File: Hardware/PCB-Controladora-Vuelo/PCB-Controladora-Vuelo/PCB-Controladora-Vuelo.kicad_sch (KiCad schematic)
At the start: 14 parts, among them J1 Jumper Serial, J2 CONN, U1 MPU-5060, U2 ESP32-DEVKIT-V1, U2 Nrf24l01, U3 AMS1117-3.3

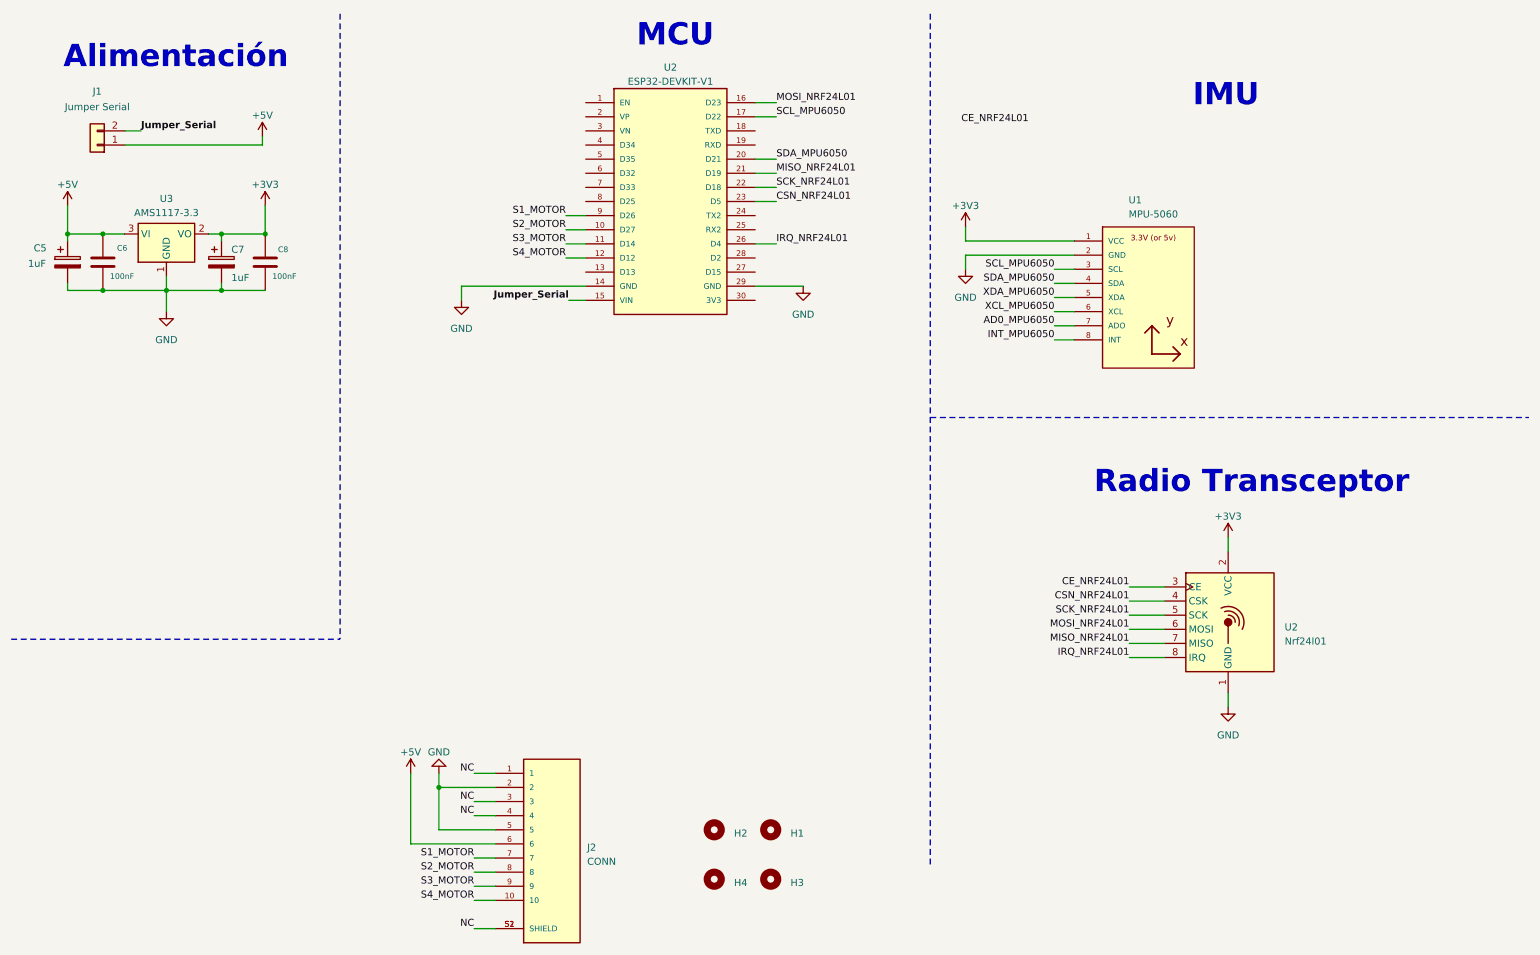
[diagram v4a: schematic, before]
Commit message: subo cambios hechos en legui solucione mpu y lugar esp32 mal Footprints
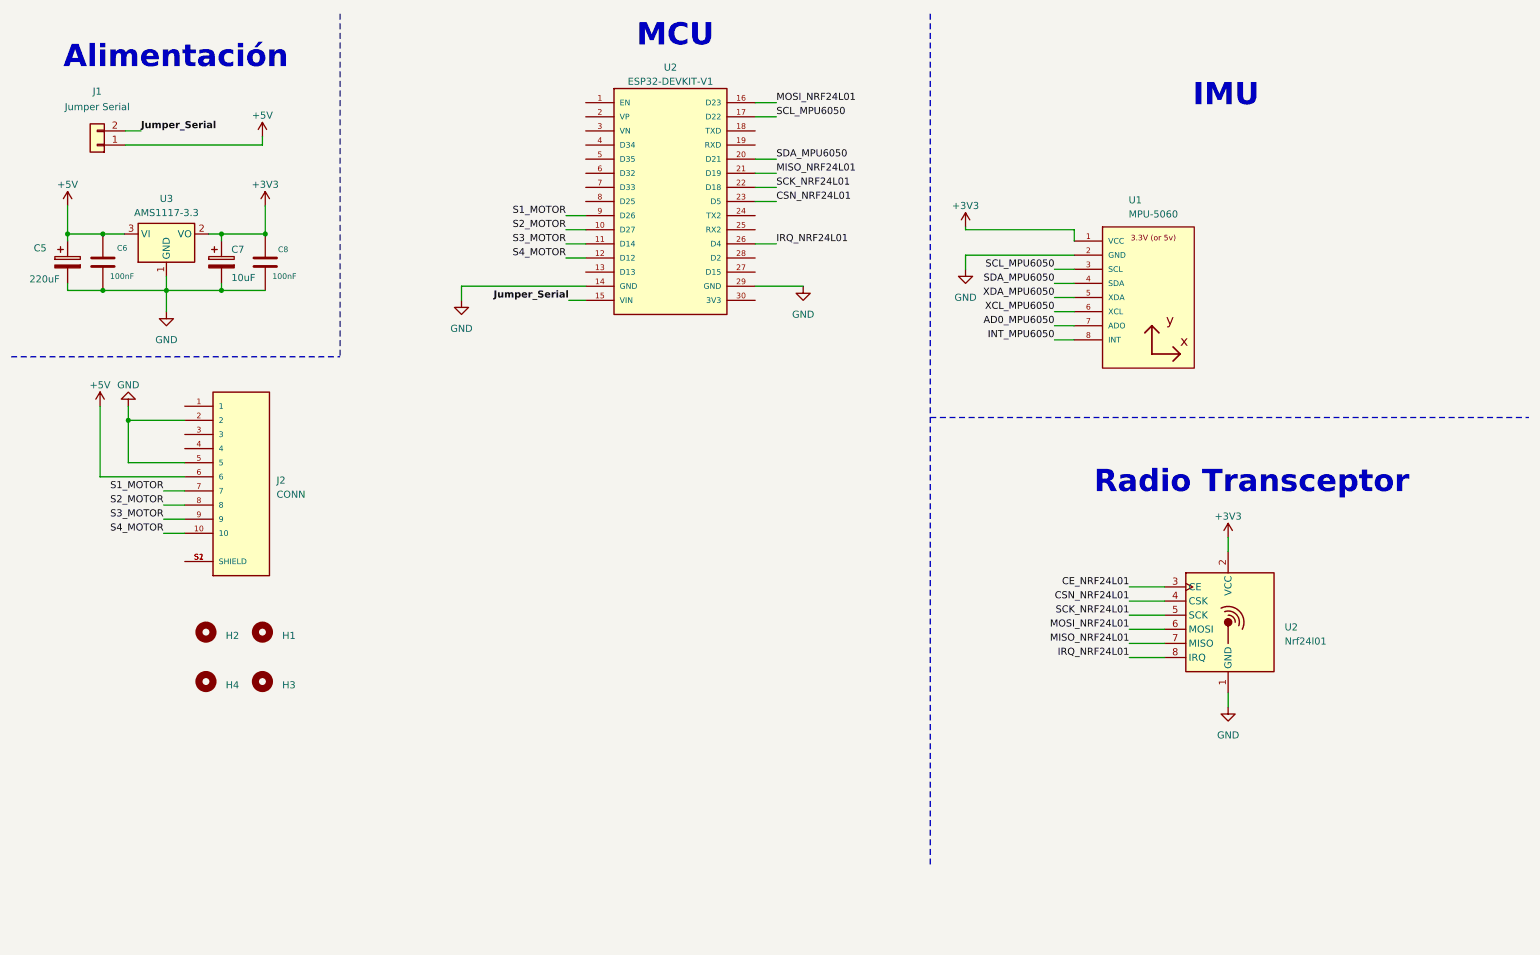
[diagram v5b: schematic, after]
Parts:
- C5: value 1uF -> 220uF
- C7: value 1uF -> 10uF
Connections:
- removed net NC: J2.1, J2.3, J2.4, J2.S1 (SHIELD), J2.S2 (SHIELD)
- new net: J2.S1 (SHIELD), J2.S2 (SHIELD)
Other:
- moved on the sheet: H1, H2, H3, H4, J2

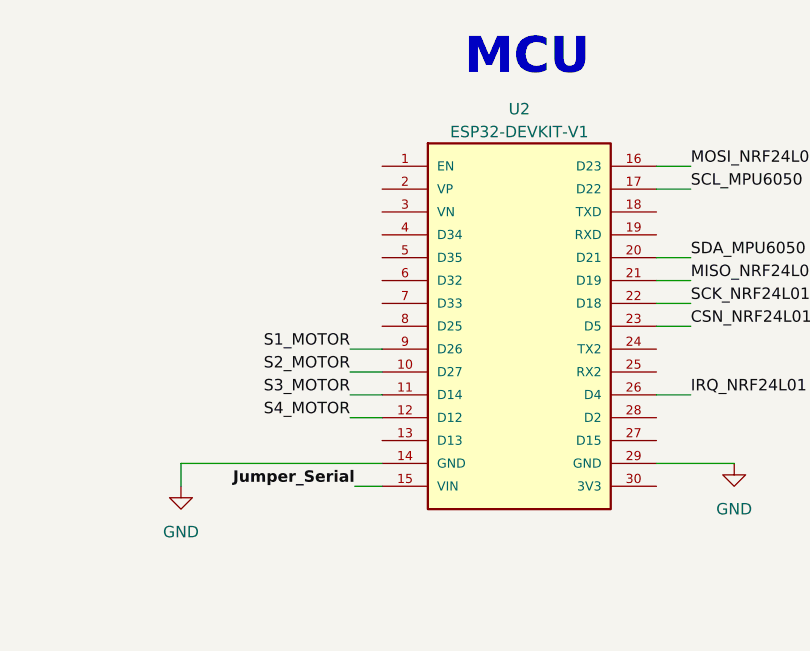
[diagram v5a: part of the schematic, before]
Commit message: Realice cambios de huella ESP32 y Symbol
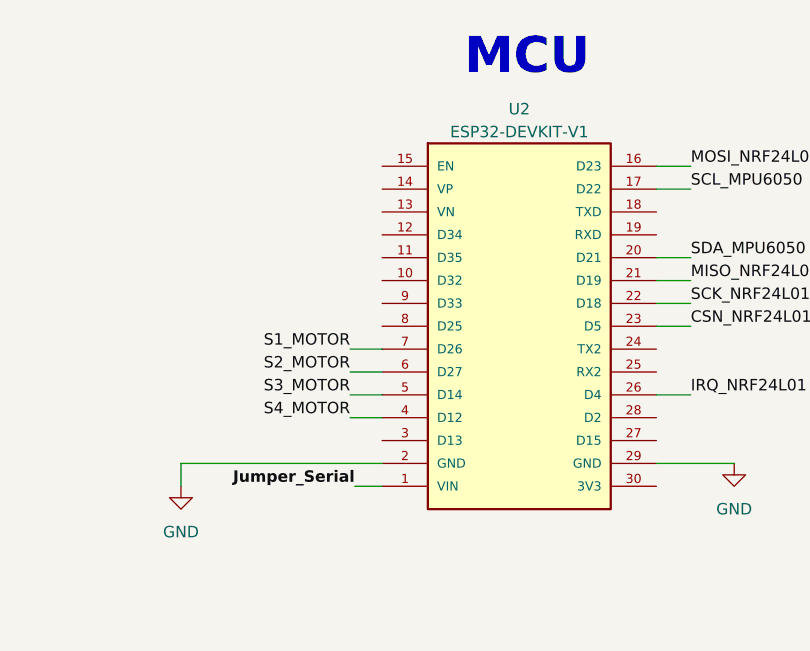
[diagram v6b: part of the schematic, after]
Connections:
- net GND: now also U2.2 (GND); no longer U2.14 (GND)
- net Jumper_Serial: now also U2.1 (VIN); no longer U2.15 (VIN)
- net S1_MOTOR: now also U2.7 (D26); no longer U2.9 (D26)
- net S2_MOTOR: now also U2.6 (D27); no longer U2.10 (D27)
- net S3_MOTOR: now also U2.5 (D14); no longer U2.11 (D14)
- net S4_MOTOR: now also U2.4 (D12); no longer U2.12 (D12)
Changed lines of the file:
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@@
       (effects (font (size 1.27 1.27)))
     )
-    (property "Footprint" "Footprints:ESP32-DEVKIT-V1-30Pines" (at 131.826 48.26 0)
+    (property "Footprint" "Footprints:ESP32-DEVKIT-V1-30Pines" (at 134.366 41.91 0)
       (effects (font (size 1.27 1.27)) (justify bottom) hide)
     )

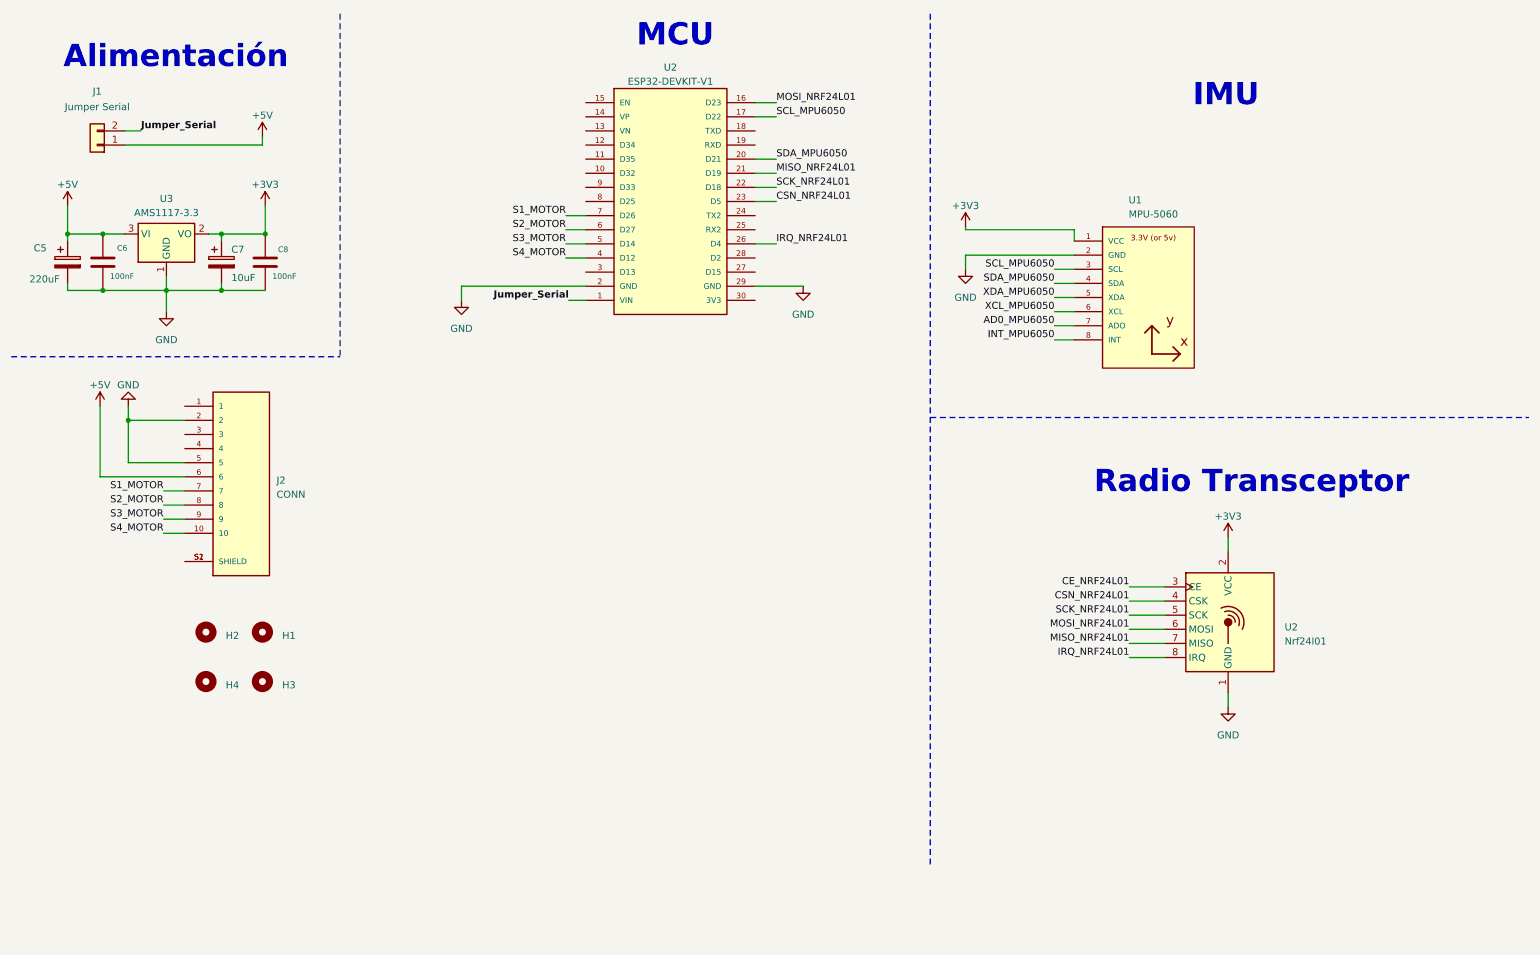
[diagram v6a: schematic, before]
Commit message: muchos cambios leer saque todos los NC y coloque X ya que al poner etiquetas nc reconoce como que debe haber una conexion entre ellos y nqv tambien digamos que hice una buena 1ra parte de pcb, que se debe corregir y mirar todo mas a detalle , faltan definir unos pines para ver si es necesario para la primera prueba xD
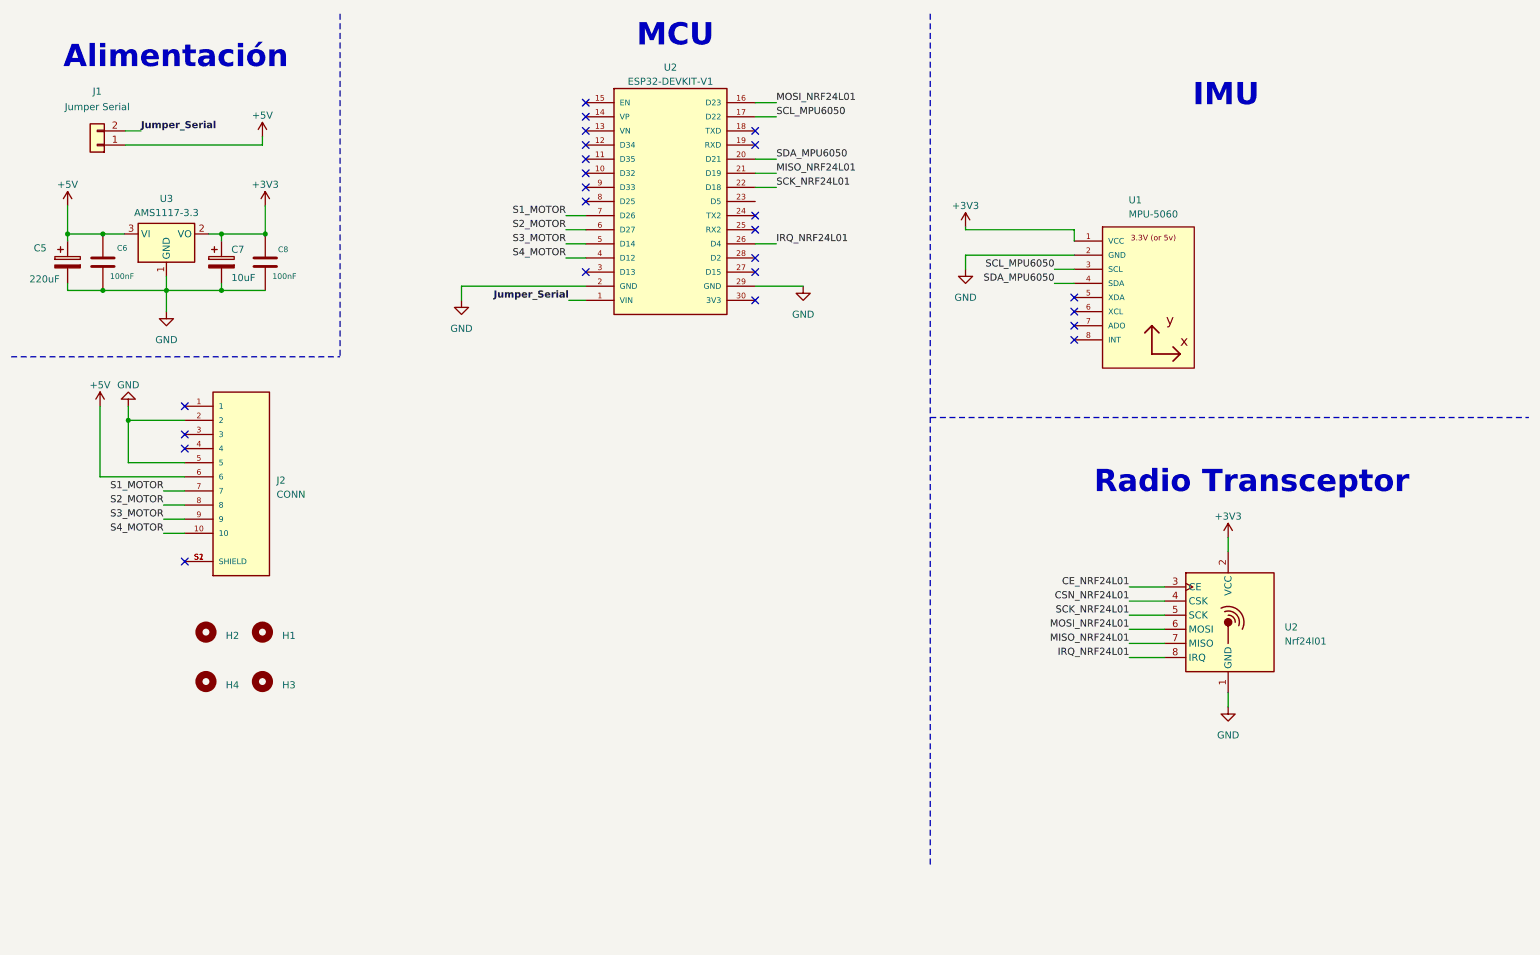
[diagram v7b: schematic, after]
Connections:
- net CSN_NRF24L01: no longer U2.23 (D5)
- net AD0_MPU6050: no longer names the net of U1.7 (ADO)
- net INT_MPU6050: no longer names the net of U1.8 (INT)
- net XCL_MPU6050: no longer names the net of U1.6 (XCL)
- net XDA_MPU6050: no longer names the net of U1.5 (XDA)
- no-connect marks 0 -> 24
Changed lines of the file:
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@@
   (junction (at 49.784 51.562) (diameter 0) (color 0 0 0 0)
   )
+  (no_connect (at 145.796 63.5))
+  (no_connect (at 115.316 30.48))
+  (no_connect (at 43.18 82.55))
+  (no_connect (at 115.316 35.56))
+  (no_connect (at 145.796 58.42))
+  (no_connect (at 115.316 40.64))
+  (no_connect (at 115.316 45.72))
+  (no_connect (at 145.796 33.02))
+  (no_connect (at 115.316 38.1))
+  (no_connect (at 115.316 33.02))
+  (no_connect (at 203.2 65.532))
+  (no_connect (at 145.796 35.56))
+  (no_connect (at 115.316 27.94))
+  (no_connect (at 115.316 43.18))
+  (no_connect (at 145.796 55.88))
+  (no_connect (at 203.2 68.072))
+  (no_connect (at 43.18 90.17))
+  (no_connect (at 203.2 62.992))
+  (no_connect (at 43.18 87.63))
+  (no_connect (at 43.18 110.49))
+  (no_connect (at 203.2 70.612))
+  (no_connect (at 115.316 58.42))
+  (no_connect (at 145.796 48.26))
+  (no_connect (at 145.796 50.8))
   (wire (pts (xy 213.106 120.142) (xy 219.456 120.142))
     (stroke (width 0) (type default))
   )
-  (wire (pts (xy 199.644 65.532) (xy 203.2 65.532))
-    (stroke (width 0) (type default))
-  )
   (wire (pts (xy 149.606 38.1) (xy 145.796 38.1))
     (stroke (width 0) (type default))
@@
     (stroke (width 0) (type default))
   )
-  (wire (pts (xy 145.796 45.72) (xy 149.606 45.72))
-    (stroke (width 0) (type default))
-  )
   (wire (pts (xy 22.098 51.562) (xy 22.098 52.832))
     (stroke (width 0) (type default))
   )
-  (wire (pts (xy 199.644 68.072) (xy 203.2 68.072))
-    (stroke (width 0) (type default))
-  )
   (wire (pts (xy 199.644 60.452) (xy 203.2 60.452))
     (stroke (width 0) (type default))
@@
     (stroke (width 0) (type default))
   )
-  (wire (pts (xy 203.2 70.612) (xy 199.644 70.612))
-    (stroke (width 0) (type default))
-  )
   (wire (pts (xy 213.106 122.682) (xy 219.456 122.682))
     (stroke (width 0) (type default))
@@
     (stroke (width 0) (type default))
   )
-  (wire (pts (xy 199.644 62.992) (xy 203.2 62.992))
-    (stroke (width 0) (type default))
-  )
   (wire (pts (xy 33.02 92.71) (xy 33.02 85.09))
     (stroke (width 0) (type default))
@@
     (effects (font (size 1.27 1.27)) (justify right bottom))
   )
-  (label "XCL_MPU6050" (at 199.644 65.532 180) (fields_autoplaced)
-    (effects (font (size 1.27 1.27)) (justify right bottom))
-  )
   (label "S3_MOTOR" (at 111.76 53.34 180) (fields_autoplaced)
     (effects (font (size 1.27 1.27)) (justify right bottom))
@@
     (effects (font (size 1.27 1.27)) (justify left bottom))
   )
-  (label "INT_MPU6050" (at 199.644 70.612 180) (fields_autoplaced)
-    (effects (font (size 1.27 1.27)) (justify right bottom))
-  )
   (label "SCL_MPU6050" (at 199.644 57.912 180) (fields_autoplaced)
     (effects (font (size 1.27 1.27)) (justify right bottom))
@@
     (effects (font (size 1.27 1.27) bold) (justify right bottom))
   )
-  (label "CSN_NRF24L01" (at 149.606 45.72 0) (fields_autoplaced)
-    (effects (font (size 1.27 1.27)) (justify left bottom))
-  )
   (label "MOSI_NRF24L01" (at 149.606 27.94 0) (fields_autoplaced)
     (effects (font (size 1.27 1.27)) (justify left bottom))
@@
     (effects (font (size 1.27 1.27)) (justify right bottom))
   )
-  (label "XDA_MPU6050" (at 199.644 62.992 180) (fields_autoplaced)
-    (effects (font (size 1.27 1.27)) (justify right bottom))
-  )
   (label "S4_MOTOR" (at 39.37 105.41 180) (fields_autoplaced)
     (effects (font (size 1.27 1.27)) (justify right bottom))
@@
     (effects (font (size 1.27 1.27)) (justify left bottom))
   )
-  (label "AD0_MPU6050" (at 199.644 68.072 180) (fields_autoplaced)
-    (effects (font (size 1.27 1.27)) (justify right bottom))
-  )
   (label "S1_MOTOR" (at 39.37 97.79 180) (fields_autoplaced)

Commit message: Trabaje en el PCB corriegindo ordenes faltaria ver si se pueden agregar pines y corregir que no existan riesgo al momento de planchar o por un corto o abrirse el circuito
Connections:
- no-connect marks 24 -> 25
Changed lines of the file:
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@@
   (no_connect (at 43.18 110.49))
   (no_connect (at 203.2 70.612))
+  (no_connect (at 145.796 45.72))
   (no_connect (at 115.316 58.42))
   (no_connect (at 145.796 48.26))
